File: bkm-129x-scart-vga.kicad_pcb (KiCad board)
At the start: 2 copper layers, 105 x 160 mm, 67 parts, among them J1 DB15_Female_HighDensity_Mount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, J2 SCART-F, J3 SJ1-353XNG, J5 Conn_02x32_Row_Letter_Last, J6 ICSP, Q1 DTC144EKA, Q2 MMBT3904, SW1 PBH4UEENAGX, SW2 PBH4UEENAGX, U1 ADG1611, U101 LDL1117S50R, U2 THS7374, U3 arduino-nano-v3, U4 74LVC125, U5 MIC3490-5.0, U6 ATMEGA328PB-AU, Y1 CSTNE16M0VH3L000R0

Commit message: Convert to KiCad 8.0.
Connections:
- net ~BX_OE renamed ~{BX_OE}
- net ~EXT_SYNC_OE renamed ~{EXT_SYNC_OE}
- net ~MCU_RESET renamed ~{MCU_RESET}
- net ~MCU_SS renamed ~{MCU_SS}
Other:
- net class Default removed

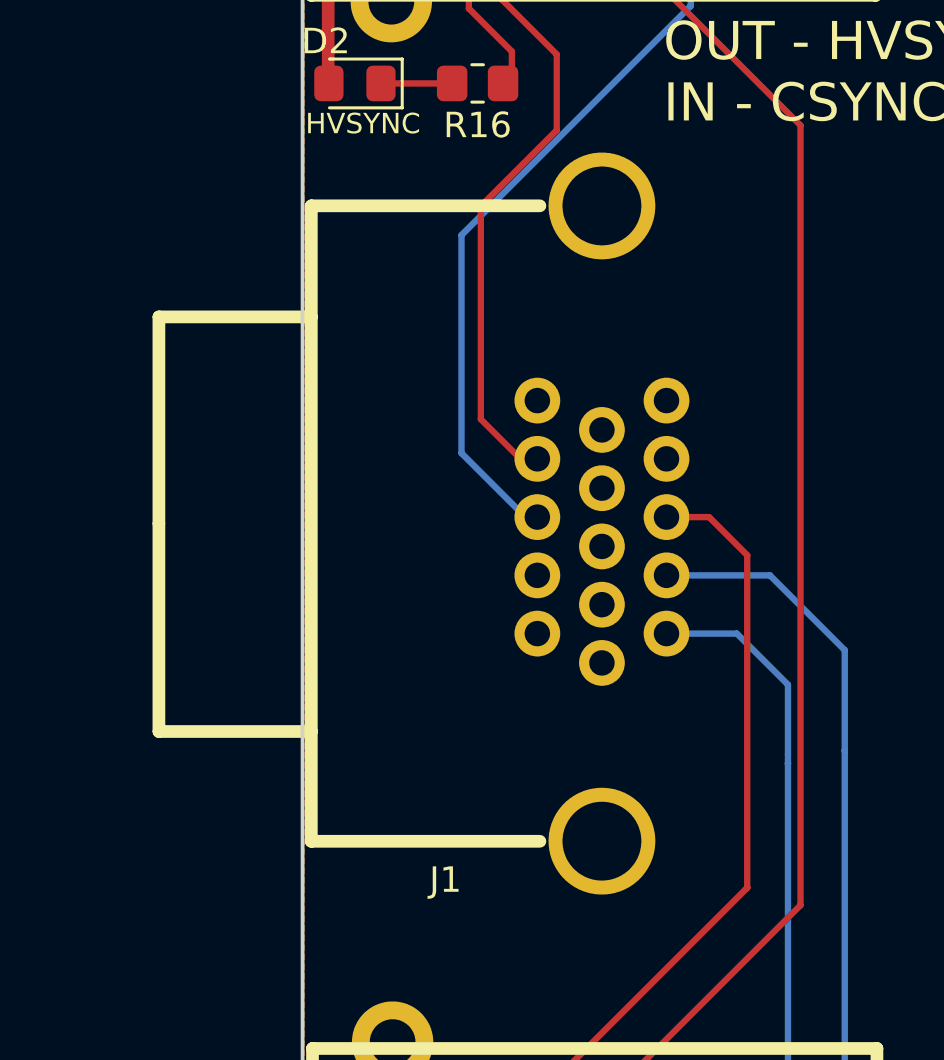
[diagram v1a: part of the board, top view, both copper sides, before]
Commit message: Edit J1 VGA DB15: Move X -0.7775 mm Edit footprint silkscreen matching board edge Change mounting holes to: Pad shape: Rectangular 4.2 x 4.2, Hole shape: Oval 3.2 x 2.2.
Unfill all zones.
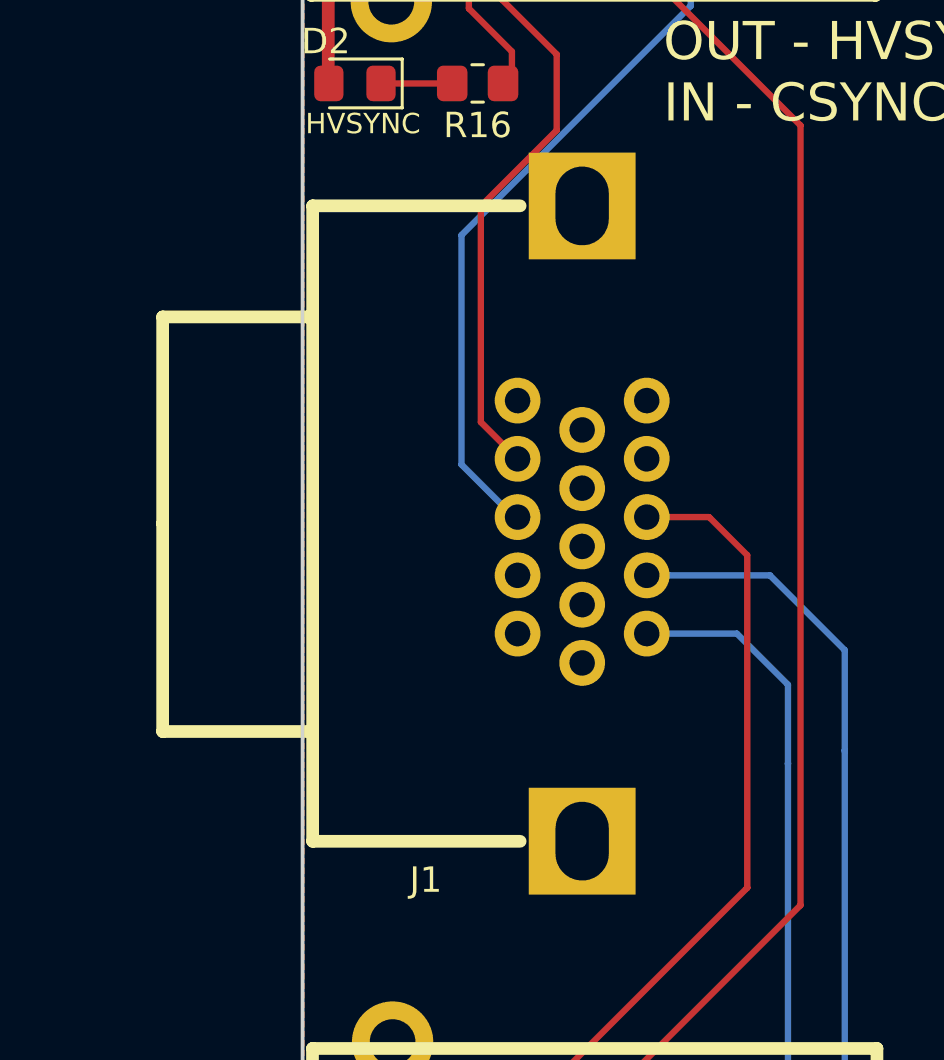
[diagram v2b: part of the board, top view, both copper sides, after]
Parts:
- moved J1 0.78 mm to (60.5, 65.8)
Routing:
- net /VGA_G: track 29.9 -> 31.4 mm
- net /VGA_R: track 22.7 -> 23.9 mm
- net /VGA_B: track 31.6 -> 32.4 mm
- net /V_SYNC: track 27.1 -> 26.4 mm
- net /H_SYNC: track 31.2 -> 30.7 mm
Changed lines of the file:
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@@
 	(footprint "HD15-VGA:HD15-VGA"
 		(layer "F.Cu")
-		(at 61.2775 65.8241 -90)
+		(at 60.5 65.8241 -90)
 		(property "Reference" "J1"
-			(at 14.02 6.15 0)
+			(at 14.02 6.15 180)
 			(layer "F.SilkS")
 			(effects
@@
 		)
 		(property "Value" "DB15_Female_HighDensity_MountingHoles"
-			(at 0.0508 7.9756 -90)
+			(at 0.0508 7.9756 90)
 			(layer "F.Fab")
 			(effects
@@
 		(attr through_hole)
 		(fp_line
-			(start -8.128 17.4244)
-			(end -8.128 11.43)
+			(start -8.128 16.5)
+			(end -8.128 10.6)
 			(stroke
 				(width 0.5)
@@
 		)
 		(fp_line
-			(start 0 17.4244)
-			(end -8.128 17.4244)
+			(start 0 16.5)
+			(end -8.128 16.5)
 			(stroke
 				(width 0.5)
@@
 		)
 		(fp_line
-			(start 0 17.4244)
-			(end 8.1788 17.4244)
+			(start 0 16.5)
+			(end 8.1788 16.5)
 			(stroke
 				(width 0.5)
@@
 		)
 		(fp_line
-			(start 8.1788 17.4244)
-			(end 8.1788 11.43)
+			(start 8.1788 16.5)
+			(end 8.1788 10.6)
 			(stroke
 				(width 0.5)
@@
 		)
 		(fp_line
-			(start -12.4968 11.43)
-			(end 12.4968 11.43)
+			(start -12.4968 10.6)
+			(end 12.4968 10.6)
 			(stroke
 				(width 0.5)
@@
 		)
 		(fp_line
-			(start -12.4968 11.43)
+			(start -12.4968 10.6)
 			(end -12.4968 2.4384)
 			(stroke
@@
 		)
 		(fp_line
-			(start 12.4968 11.43)
+			(start 12.4968 10.6)
 			(end 12.4968 2.4384)
 			(stroke
@@
 			(layer "F.SilkS")
 		)
-		(pad "0" thru_hole circle
+		(pad "0" thru_hole rect
 			(at -12.49172 0 270)
 			(size 4.2 4.2)
-			(drill 3.1)
+			(drill oval 3.1 2.1)
 			(layers "*.Cu" "*.Mask")
 			(remove_unused_layers no)
 			(net 6 "GND")
 		)
-		(pad "0" thru_hole circle
+		(pad "0" thru_hole rect
 			(at 12.49172 0 270)
 			(size 4.2 4.2)
-			(drill 3.1)
+			(drill oval 3.1 2.1)
 			(layers "*.Cu" "*.Mask")
 			(remove_unused_layers no)
@@
 	)
 	(segment
-		(start 67.88658 67.86118)
-		(end 70.8279 70.8025)
+		(start 70.8279 74.7395)
+		(end 70.8279 74.7776)
 		(width 0.25)
 		(layer "B.Cu")
@@
 	)
 	(segment
-		(start 70.8279 70.8025)
-		(end 70.8279 74.7395)
+		(start 70.8279 89.1356)
+		(end 68.5943 91.3692)
 		(width 0.25)
 		(layer "B.Cu")
@@
 	)
 	(segment
-		(start 70.8279 74.7395)
-		(end 70.8279 74.7776)
+		(start 67.88658 67.86118)
+		(end 70.8279 70.8025)
 		(width 0.25)
 		(layer "B.Cu")
@@
 	)
 	(segment
-		(start 70.8279 89.1356)
-		(end 68.5943 91.3692)
+		(start 70.8279 70.8025)
+		(end 70.8279 74.7395)
 		(width 0.25)
 		(layer "B.Cu")
@@
 	)
 	(segment
-		(start 63.8175 67.86118)
-		(end 63.91148 67.86118)
+		(start 70.8279 74.7395)
+		(end 70.8279 89.1356)
 		(width 0.25)
 		(layer "B.Cu")
@@
 	)
 	(segment
-		(start 70.8279 74.7395)
-		(end 70.8279 89.1356)
+		(start 63.04 67.86118)
+		(end 63.91148 67.86118)
 		(width 0.25)
 		(layer "B.Cu")
@@
 	)
 	(segment
-		(start 63.8175 67.86118)
+		(start 63.04 67.86118)
 		(end 67.88658 67.86118)
 		(width 0.25)
@@
 	)
 	(segment
-		(start 65.4939 65.5701)
-		(end 66.9925 67.0687)
+		(start 61.0943 91.3692)
+		(end 61.0943 91.3457)
 		(width 0.25)
 		(layer "F.Cu")
@@
 	)
 	(segment
-		(start 66.9925 67.0687)
-		(end 66.9925 80.1497)
+		(start 63.04 65.5701)
+		(end 65.4939 65.5701)
 		(width 0.25)
 		(layer "F.Cu")
@@
 	)
 	(segment
-		(start 61.0943 91.3692)
-		(end 61.0943 91.3457)
+		(start 65.4939 65.5701)
+		(end 66.9925 67.0687)
 		(width 0.25)
 		(layer "F.Cu")
@@
 	)
 	(segment
-		(start 63.8175 65.5701)
-		(end 65.4939 65.5701)
+		(start 66.9925 67.0687)
+		(end 66.9925 80.1497)
 		(width 0.25)
 		(layer "F.Cu")
@@
 	)
 	(segment
-		(start 68.5943 74.9189)
-		(end 68.5943 75.2475)
-		(width 0.25)
-		(layer "B.Cu")
-		(net 36)
-	)
-	(segment
-		(start 66.58356 70.15226)
-		(end 68.5943 72.163)
-		(width 0.25)
-		(layer "B.Cu")
-		(net 36)
-	)
-	(segment
-		(start 68.5943 72.163)
-		(end 68.5943 74.9189)
+		(start 68.5943 75.2475)
+		(end 68.5943 75.2872)
 		(width 0.25)
 		(layer "B.Cu")
@@
 	(segment
 		(start 68.5943 75.2475)
-		(end 68.5943 75.2872)
+		(end 68.5943 88.8692)
 		(width 0.25)
 		(layer "B.Cu")
@@
 	)
 	(segment
-		(start 68.5943 75.2475)
-		(end 68.5943 88.8692)
+		(start 68.5943 72.163)
+		(end 68.5943 75.2475)
 		(width 0.25)
 		(layer "B.Cu")
@@
 	)
 	(segment
-		(start 63.8175 70.15226)
+		(start 63.04 70.15226)
 		(end 66.58356 70.15226)
 		(width 0.25)
@@
 	)
 	(segment
-		(start 63.8175 70.15226)
+		(start 63.04 70.15226)
 		(end 63.82766 70.15226)
 		(width 0.25)
@@
 	)
 	(segment
-		(start 63.8175 70.15226)
-		(end 63.8175 70.5104)
+		(start 66.58356 70.15226)
+		(end 68.5943 72.163)
 		(width 0.25)
 		(layer "B.Cu")
@@
 	)
 	(segment
-		(start 64.77 45.466)
-		(end 64.77 41.4221)
+		(start 57.96 65.5701)
+		(end 57.8201 65.5701)
 		(width 0.25)
 		(layer "B.Cu")
@@
 	)
 	(segment
-		(start 58.2676 65.5701)
-		(end 55.753 63.0555)
+		(start 57.8201 65.5701)
+		(end 55.753 63.503)
 		(width 0.25)
 		(layer "B.Cu")
@@
 	)
 	(segment
-		(start 58.7375 65.5701)
-		(end 58.2676 65.5701)
+		(start 55.753 54.483)
+		(end 64.77 45.466)
 		(width 0.25)
 		(layer "B.Cu")
@@
 	)
 	(segment
-		(start 64.77 41.4221)
-		(end 66.0435 40.1486)
+		(start 55.753 63.503)
+		(end 55.753 54.483)
 		(width 0.25)
 		(layer "B.Cu")
@@
 	)
 	(segment
-		(start 55.753 54.483)
-		(end 64.77 45.466)
+		(start 64.77 41.4221)
+		(end 66.0435 40.1486)
 		(width 0.25)
 		(layer "B.Cu")
@@
 	)
 	(segment
-		(start 55.753 63.0555)
-		(end 55.753 54.483)
+		(start 64.77 45.466)
+		(end 64.77 41.4221)
 		(width 0.25)
 		(layer "B.Cu")
@@
 	)
 	(segment
-		(start 56.515 61.722)
-		(end 58.07202 63.27902)
+		(start 59.4995 47.371)
+		(end 59.4995 50.3555)
 		(width 0.25)
 		(layer "F.Cu")
@@
 	)
 	(segment
-		(start 57.3405 41.275)
-		(end 57.3405 45.212)
+		(start 59.4995 50.3555)
+		(end 56.515 53.34)
 		(width 0.25)
 		(layer "F.Cu")
@@
 	)
 	(segment
-		(start 59.4995 50.3555)
-		(end 56.515 53.34)
-		(width 0.25)
-		(layer "F.Cu")
-		(net 50)
-	)
-	(segment
-		(start 58.5435 40.1486)
-		(end 58.4669 40.1486)
+		(start 57.3405 41.275)
+		(end 57.3405 45.212)
 		(width 0.25)
 		(layer "F.Cu")
@@
 	)
 	(segment
-		(start 58.07202 63.27902)
-		(end 58.7375 63.27902)
+		(start 56.515 53.34)
+		(end 56.515 61.83402)
 		(width 0.25)
 		(layer "F.Cu")
@@
 	)
 	(segment
-		(start 58.4669 40.1486)
-		(end 57.3405 41.275)
+		(start 56.515 61.83402)
+		(end 57.96 63.27902)
 		(width 0.25)
 		(layer "F.Cu")
@@
 	)
 	(segment
-		(start 56.515 53.34)
-		(end 56.515 61.722)
+		(start 58.5435 40.1486)
+		(end 58.4669 40.1486)
 		(width 0.25)
 		(layer "F.Cu")
@@
 	)
 	(segment
-		(start 59.4995 47.371)
-		(end 59.4995 50.3555)
+		(start 58.4669 40.1486)
+		(end 57.3405 41.275)
 		(width 0.25)
 		(layer "F.Cu")
@@
 		(min_thickness 0.254)
 		(filled_areas_thickness no)
-		(fill yes
+		(fill
 			(thermal_gap 0.508)
 			(thermal_bridge_width 0.508)
@@
 		(min_thickness 0.254)
 		(filled_areas_thickness no)
-		(fill yes
+		(fill
 			(thermal_gap 0.508)
 			(thermal_bridge_width 0.508)

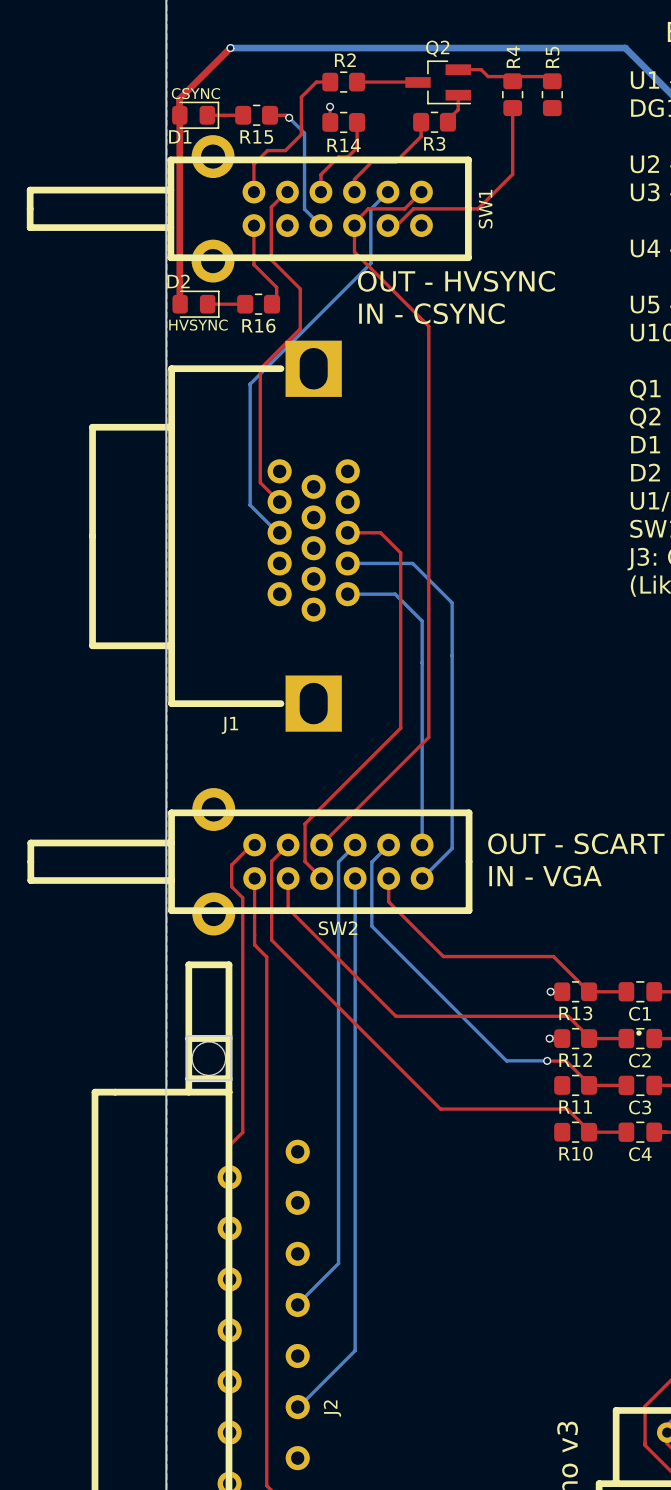
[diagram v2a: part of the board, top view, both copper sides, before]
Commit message: Edit SW1, SW2: Move X 0.4 mm Remove mounting holes
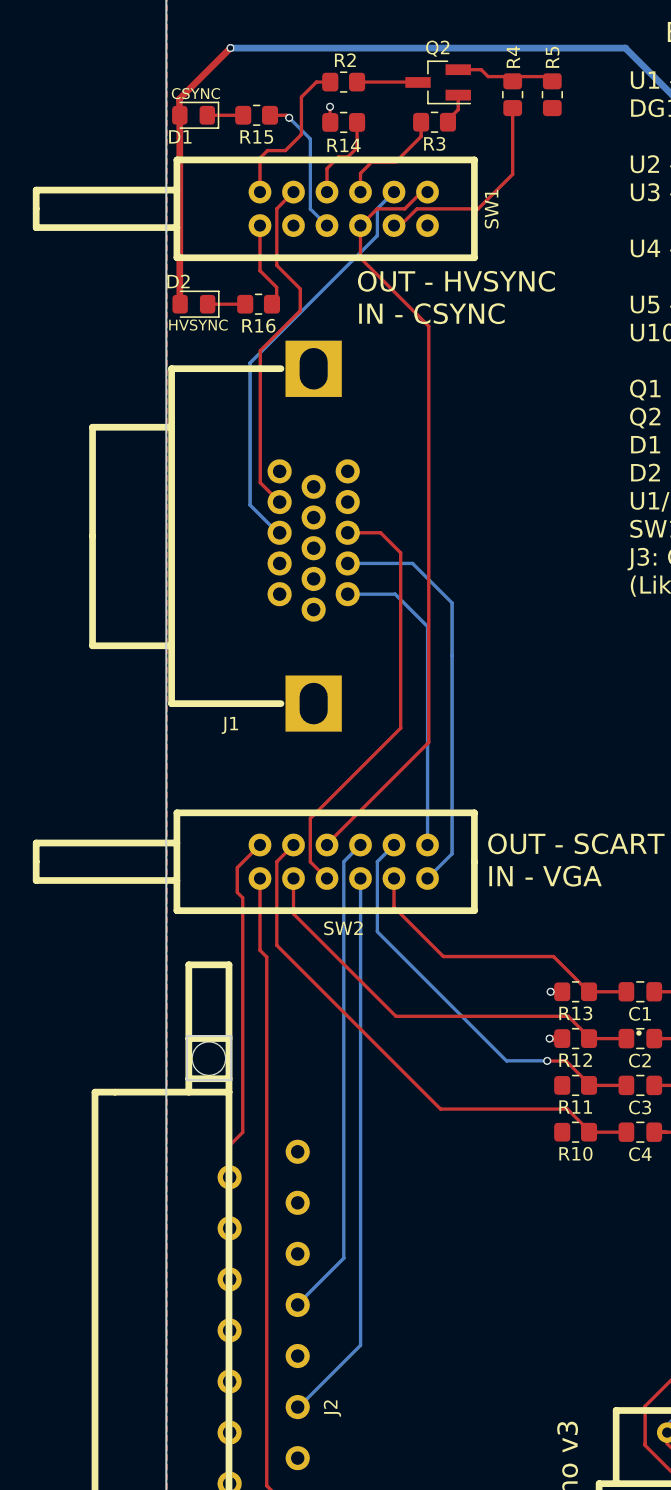
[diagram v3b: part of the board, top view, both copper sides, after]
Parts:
- moved SW1 0.45 mm to (62.7, 41.4)
- moved SW2 0.40 mm to (62.7, 90.1)

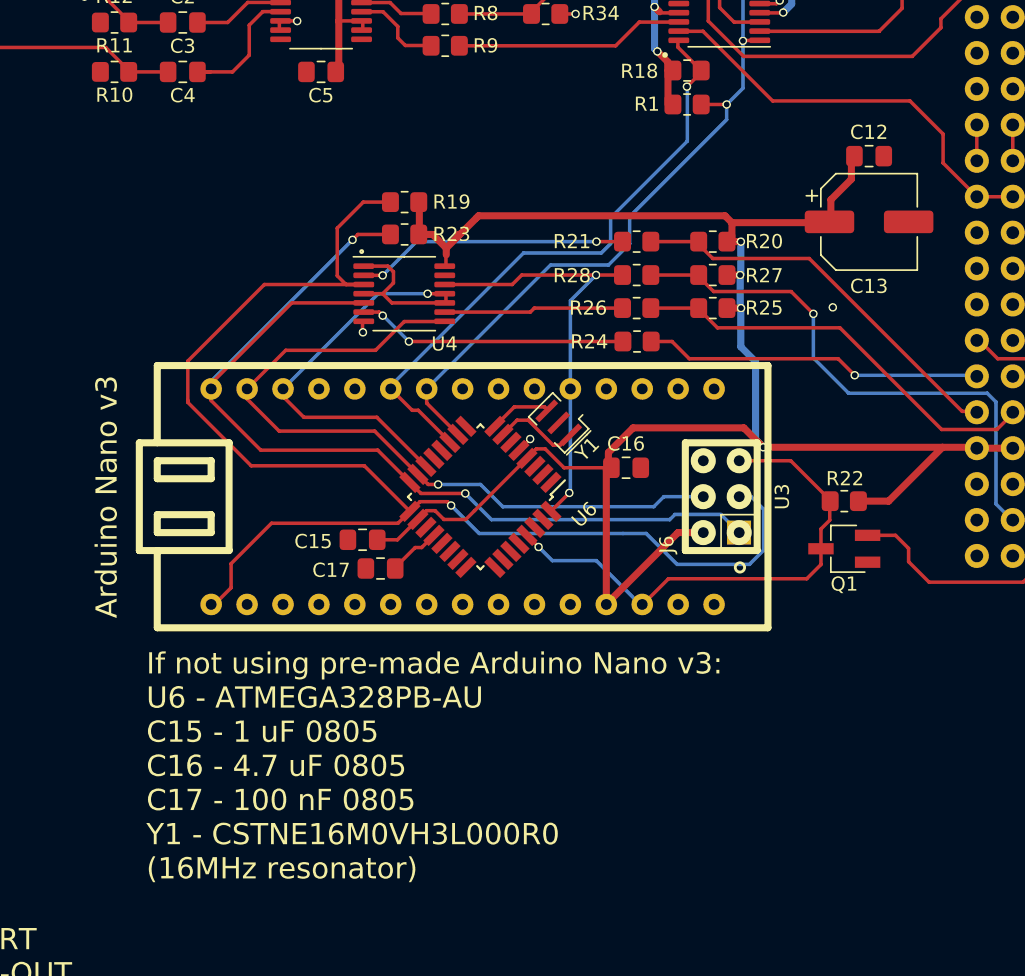
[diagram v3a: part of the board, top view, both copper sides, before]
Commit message: Remove U3 Arduino Nano from PCB and schematic.
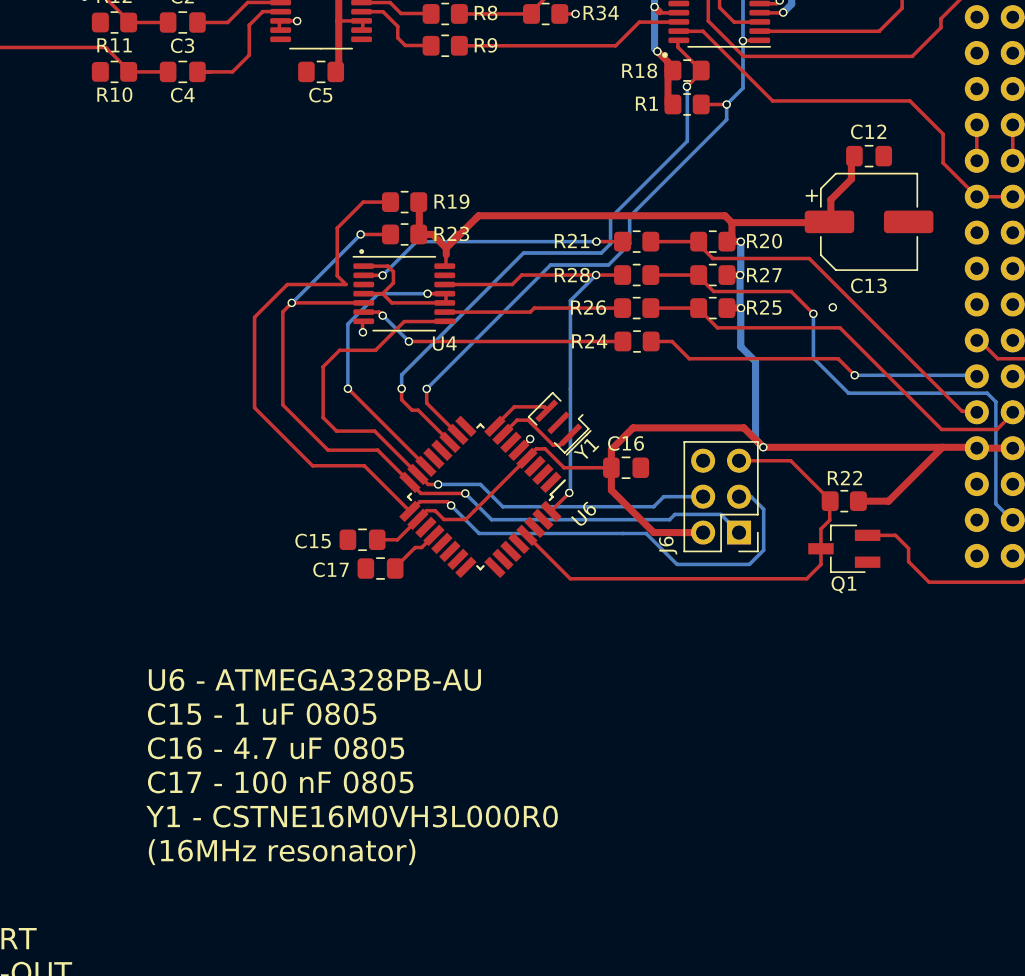
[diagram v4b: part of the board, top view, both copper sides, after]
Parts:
- removed U3: arduino-nano-v3, arduino-nano-v3:arduino-nano-v3
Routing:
- net MCU_SCK: track 96.3 -> 68.8 mm
- net MCU_MISO: track 73.0 -> 57.4 mm, vias 2 -> 3
- net +5VD: track 135.6 -> 126.3 mm
- net MCU_MOSI: track 52.5 -> 43.4 mm
- net ~{MCU_SS}: track 38.0 -> 31.2 mm, vias 1 -> 2
- net ~{MCU_RESET}: track 36.4 -> 34.9 mm, vias 1 -> 0
- net ~{EXT_SYNC_OE}: track 43.4 -> 42.8 mm, vias 1 -> 2
- net ~{BX_OE}: vias 4 -> 5
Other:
- board text added: "U6 - ATMEGA328PB-AU C15 - 1 uF 0805 C16 - 4.7 uF 0805 C17 - 100 nF 0805 Y1 - CSTNE16M0VH3L000R0 (16MHz resonator)"
- board text removed: "If not using pre-made Arduino Nano v3: U6 - ATMEGA328PB-AU C15 - 1 uF 0805 C16 - 4.7 uF 0805 C17 - 100 nF 0805 Y1 - CSTNE16M0VH3L000R0 (16MHz resonator)"
